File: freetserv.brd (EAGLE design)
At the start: 91.4 x 82.5 mm, 70 parts, among them IC2 SN75240PW, Q1 12MHz, Q2 6MHz, U1 MCP16311-E/MS

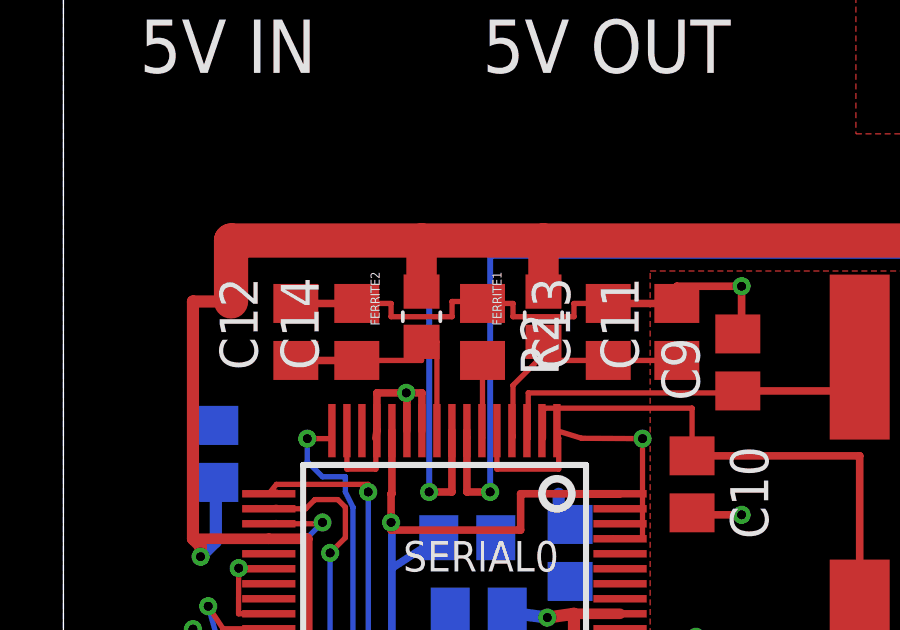
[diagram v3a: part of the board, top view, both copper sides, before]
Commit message: move 100nF capacitors closer to VPHY/VPLL
fixes #11
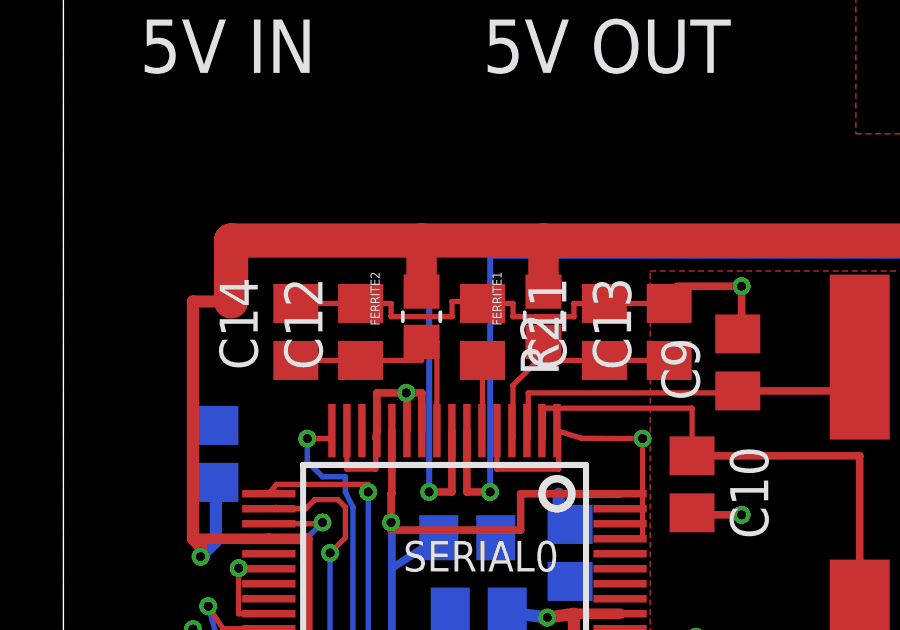
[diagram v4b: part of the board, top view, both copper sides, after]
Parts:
- moved C11 2.41 mm to (18.0, 63.8)
- moved C12 2.16 mm to (9.91, 63.8)
- moved C13 2.03 mm to (20.2, 63.8)
- moved C14 2.03 mm to (7.75, 63.8)
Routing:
- net GND: track 140.1 -> 139.2 mm
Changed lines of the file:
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@@
 <attribute name="PARTNO" value="709-1171-1-ND" x="20.955" y="58.674" size="1.778" layer="27" rot="R270" display="off"/>
 </element>
-<element name="C11" library="resistor" package="C0805" value="0.1uF" x="20.447" y="63.754" rot="R90">
-<attribute name="PARTNO" value="1276-1003-1-ND" x="20.447" y="63.754" size="1.778" layer="27" rot="R90" display="off"/>
-</element>
-<element name="C12" library="resistor" package="C0805" value="0.1uF" x="7.747" y="63.754" rot="R90">
-<attribute name="PARTNO" value="1276-1003-1-ND" x="7.747" y="63.754" size="1.778" layer="27" rot="R90" display="off"/>
-</element>
-<element name="C13" library="resistor" package="C0805" value="4.7uF" x="18.161" y="63.754" rot="R90">
-<attribute name="PARTNO" value="587-1302-1-ND" x="18.161" y="63.754" size="1.778" layer="27" rot="R90" display="off"/>
-</element>
-<element name="C14" library="resistor" package="C0805" value="4.7uF" x="9.779" y="63.754" rot="R90">
-<attribute name="PARTNO" value="587-1302-1-ND" x="9.779" y="63.754" size="1.778" layer="27" rot="R90" display="off"/>
+<element name="C11" library="resistor" package="C0805" value="0.1uF" x="18.034" y="63.754" rot="R90">
+<attribute name="PARTNO" value="1276-1003-1-ND" x="18.034" y="63.754" size="1.778" layer="27" rot="R90" display="off"/>
+</element>
+<element name="C12" library="resistor" package="C0805" value="0.1uF" x="9.906" y="63.754" rot="R90">
+<attribute name="PARTNO" value="1276-1003-1-ND" x="9.906" y="63.754" size="1.778" layer="27" rot="R90" display="off"/>
+</element>
+<element name="C13" library="resistor" package="C0805" value="4.7uF" x="20.193" y="63.754" rot="R90">
+<attribute name="PARTNO" value="587-1302-1-ND" x="20.193" y="63.754" size="1.778" layer="27" rot="R90" display="off"/>
+</element>
+<element name="C14" library="resistor" package="C0805" value="4.7uF" x="7.747" y="63.754" rot="R90">
+<attribute name="PARTNO" value="587-1302-1-ND" x="7.747" y="63.754" size="1.778" layer="27" rot="R90" display="off"/>
 </element>
 <element name="C2" library="resistor" package="C0805" value="10uF" x="30.48" y="74.295">
@@
 <contactref element="C20" pad="1"/>
 <contactref element="C21" pad="1"/>
-<wire x1="7.747" y1="64.704" x2="9.779" y2="64.704" width="0.254" layer="1"/>
 <contactref element="USB_RASPI_PWR" pad="GND"/>
 <contactref element="USB_RASPI_DATA2" pad="GND"/>
@@
 <wire x1="22.606" y1="63.688" x2="22.479" y2="63.688" width="0.254" layer="1"/>
 <wire x1="22.606" y1="65.278" x2="20.447" y2="65.278" width="0.254" layer="1"/>
-<wire x1="20.447" y1="65.278" x2="20.447" y2="64.704" width="0.254" layer="1"/>
-<wire x1="20.447" y1="64.704" x2="18.161" y2="64.704" width="0.254" layer="1"/>
-<wire x1="18.161" y1="64.704" x2="17.018" y2="64.704" width="0.1778" layer="1"/>
 <wire x1="17.018" y1="64.704" x2="17.018" y2="64.262" width="0.1778" layer="1"/>
 <wire x1="17.018" y1="64.262" x2="14.986" y2="64.262" width="0.1778" layer="1"/>
@@
 <wire x1="12.954" y1="64.262" x2="10.922" y2="64.262" width="0.1778" layer="1"/>
 <wire x1="10.922" y1="64.262" x2="10.922" y2="64.704" width="0.1778" layer="1"/>
-<wire x1="10.922" y1="64.704" x2="9.779" y2="64.704" width="0.1778" layer="1"/>
 <wire x1="14.45" y1="60.464" x2="14.45" y2="59.182" width="0.1778" layer="1"/>
 <wire x1="14.45" y1="59.182" x2="16.51" y2="59.182" width="0.1778" layer="1"/>
@@
 <wire x1="16.002" y1="50.292" x2="14.224" y2="50.292" width="0.254" layer="1"/>
 <contactref element="C45" pad="2"/>
+<wire x1="10.922" y1="64.704" x2="9.906" y2="64.704" width="0.1778" layer="1"/>
+<wire x1="9.906" y1="64.704" x2="7.747" y2="64.704" width="0.1778" layer="1"/>
+<wire x1="17.018" y1="64.704" x2="18.034" y2="64.704" width="0.1778" layer="1"/>
+<wire x1="18.034" y1="64.704" x2="20.193" y2="64.704" width="0.1778" layer="1"/>
 </signal>
 <signal name="USB0_DM_P">
@@
 <contactref element="C13" pad="1"/>
 <wire x1="16.002" y1="63.4245" x2="16.002" y2="62.804" width="0.1778" layer="1"/>
-<wire x1="16.002" y1="62.804" x2="18.161" y2="62.804" width="0.1778" layer="1"/>
 <wire x1="16.002" y1="62.804" x2="15.814" y2="62.804" width="0.1778" layer="1"/>
 <wire x1="15.814" y1="62.804" x2="14.986" y2="61.976" width="0.1778" layer="1"/>
 <wire x1="14.986" y1="61.976" x2="14.986" y2="60.246" width="0.1778" layer="1"/>
 <wire x1="14.986" y1="60.246" x2="14.95" y2="60.464" width="0.1778" layer="1"/>
-<wire x1="18.161" y1="62.804" x2="20.447" y2="62.804" width="0.1778" layer="1"/>
+<wire x1="20.193" y1="62.804" x2="18.034" y2="62.804" width="0.1778" layer="1"/>
+<wire x1="18.034" y1="62.804" x2="16.002" y2="62.804" width="0.1778" layer="1"/>
 </signal>
 <signal name="N$18">
@@
 <contactref element="C12" pad="1"/>
 <contactref element="C14" pad="1"/>
-<wire x1="9.779" y1="62.804" x2="7.747" y2="62.804" width="0.254" layer="1"/>
 <wire x1="11.938" y1="63.4245" x2="12.45" y2="63.4245" width="0.1778" layer="1"/>
 <wire x1="12.45" y1="63.4245" x2="12.45" y2="60.464" width="0.1778" layer="1"/>
 <wire x1="11.938" y1="63.4245" x2="11.938" y2="62.804" width="0.1778" layer="1"/>
-<wire x1="11.938" y1="62.804" x2="9.779" y2="62.804" width="0.1778" layer="1"/>
+<wire x1="7.747" y1="62.804" x2="9.906" y2="62.804" width="0.1778" layer="1"/>
+<wire x1="9.906" y1="62.804" x2="11.938" y2="62.804" width="0.1778" layer="1"/>
 </signal>
 <signal name="N$27">

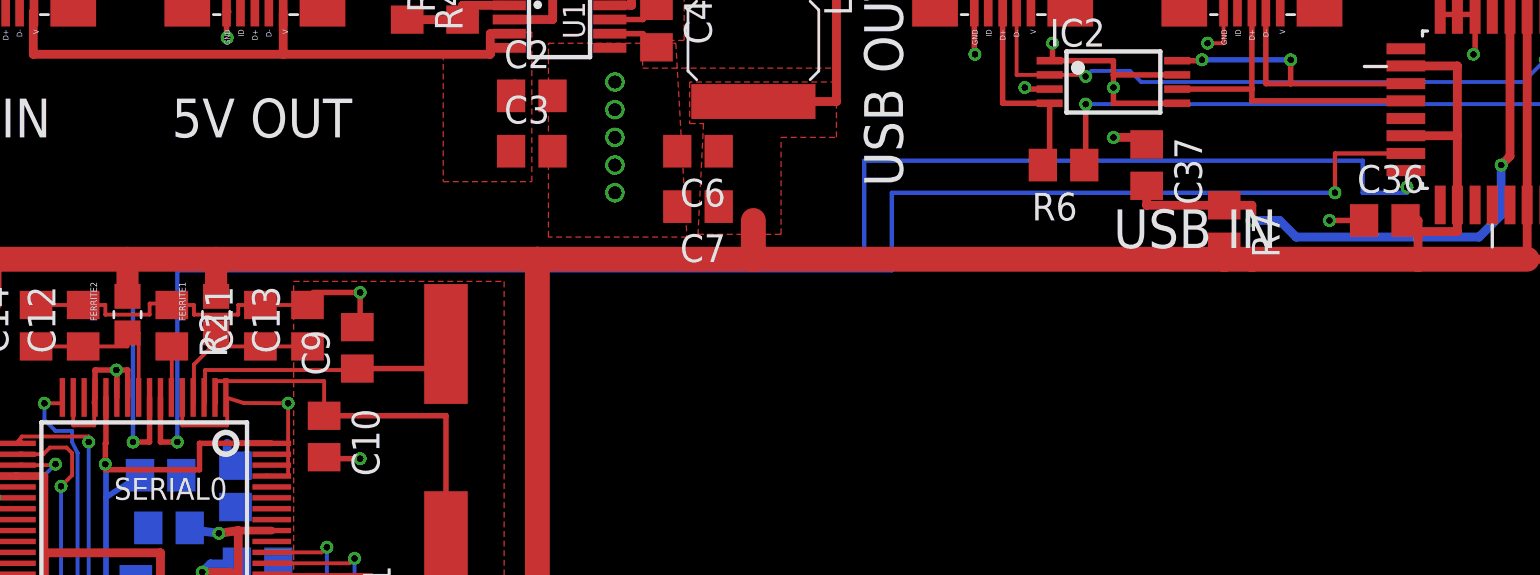
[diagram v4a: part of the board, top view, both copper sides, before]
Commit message: re-route USB as differential pairs with 45° traces
fixes #1
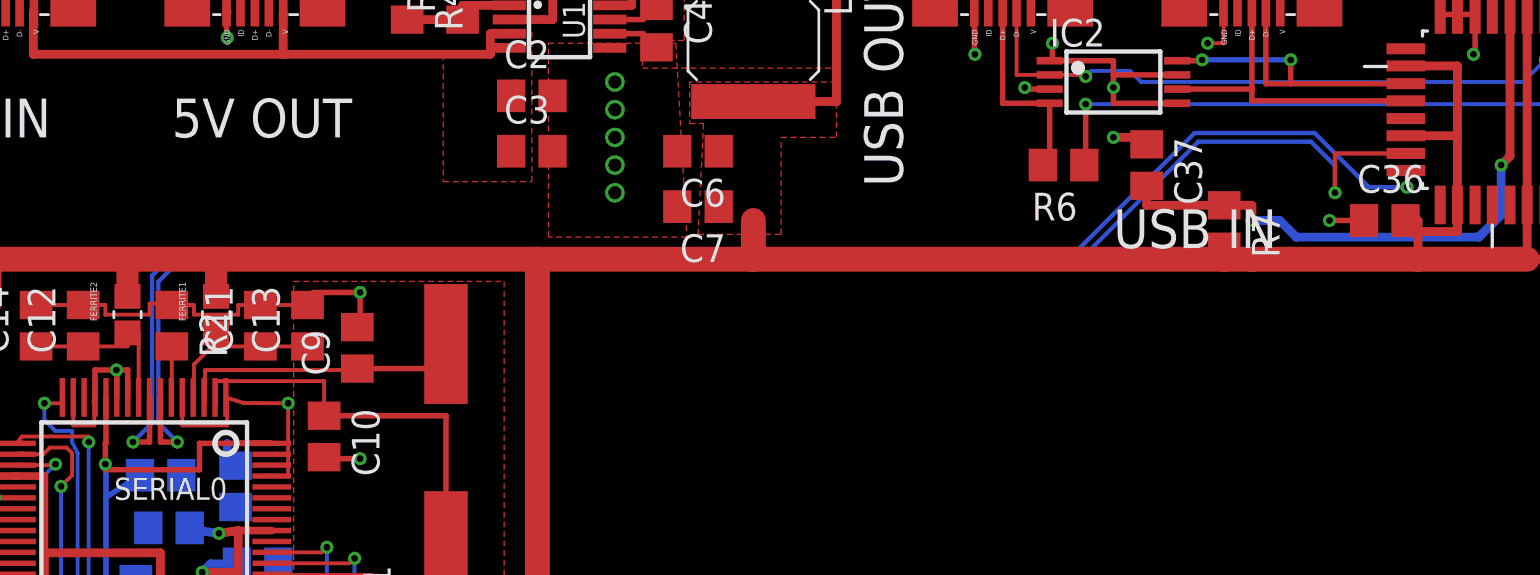
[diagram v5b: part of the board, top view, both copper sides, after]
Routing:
- net USB0_D2_P: track 76.7 -> 72.9 mm
- net USB0_D2_N: track 72.6 -> 74.2 mm
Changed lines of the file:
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@@
 <contactref element="HUB0" pad="15"/>
 <contactref element="SERIAL0" pad="7"/>
-<wire x1="46.99" y1="66.294" x2="14.224" y2="66.294" width="0.2" layer="16"/>
-<wire x1="14.224" y1="66.294" x2="14.224" y2="58.42" width="0.2" layer="16"/>
 <via x="14.224" y="58.42" extent="1-16" drill="0.3048"/>
 <wire x1="13.462" y1="60.21" x2="13.45" y2="60.464" width="0.2" layer="1"/>
 <wire x1="14.224" y1="58.42" x2="13.45" y2="58.42" width="0.254" layer="1"/>
 <wire x1="13.45" y1="58.42" x2="13.45" y2="60.464" width="0.254" layer="1"/>
-<wire x1="46.99" y1="66.294" x2="46.99" y2="69.85" width="0.2" layer="16"/>
-<wire x1="46.99" y1="69.85" x2="67.31" y2="69.85" width="0.2" layer="16"/>
 <via x="67.31" y="69.85" extent="1-16" drill="0.3048"/>
 <wire x1="67.31" y1="69.85" x2="67.31" y2="71.6534" width="0.2" layer="1"/>
 <wire x1="67.31" y1="71.6534" x2="70.5612" y2="71.6534" width="0.2" layer="1"/>
+<wire x1="67.31" y1="69.85" x2="67.31" y2="71.09115625" width="0.2" layer="16"/>
+<wire x1="67.31" y1="71.09115625" x2="66.21115625" y2="72.19" width="0.2" layer="16"/>
+<wire x1="66.21115625" y1="72.19" x2="61.04284375" y2="72.19" width="0.2" layer="16"/>
+<wire x1="61.04284375" y1="72.19" x2="55.45484375" y2="66.602" width="0.2" layer="16"/>
+<wire x1="55.45484375" y1="66.602" x2="14.17984375" y2="66.602" width="0.2" layer="16"/>
+<wire x1="14.17984375" y1="66.602" x2="13.349421875" y2="65.771578125" width="0.2" layer="16"/>
+<wire x1="13.349421875" y1="65.771578125" x2="13.349421875" y2="59.294578125" width="0.2" layer="16"/>
+<wire x1="13.349421875" y1="59.294578125" x2="14.224" y2="58.42" width="0.2" layer="16"/>
 </signal>
 <signal name="USB0_D2_P" class="1">
 <contactref element="HUB0" pad="16"/>
 <contactref element="SERIAL0" pad="8"/>
-<wire x1="45.72" y1="67.056" x2="12.192" y2="67.056" width="0.2" layer="16"/>
-<wire x1="12.192" y1="67.056" x2="12.192" y2="58.42" width="0.2" layer="16"/>
 <via x="12.192" y="58.42" extent="1-16" drill="0.3048"/>
 <wire x1="12.192" y1="58.42" x2="12.95" y2="58.42" width="0.254" layer="1"/>
 <wire x1="12.95" y1="58.42" x2="12.95" y2="60.464" width="0.254" layer="1"/>
-<wire x1="45.72" y1="67.056" x2="45.72" y2="71.32" width="0.2" layer="16"/>
-<wire x1="45.72" y1="71.32" x2="68.58" y2="71.32" width="0.2" layer="16"/>
 <via x="70.612" y="70.104" extent="1-16" drill="0.3048"/>
 <wire x1="70.612" y1="70.104" x2="70.612" y2="70.866" width="0.2" layer="1"/>
 <wire x1="70.612" y1="70.866" x2="70.5612" y2="70.866" width="0.2" layer="1"/>
-<wire x1="68.58" y1="71.32" x2="68.58" y2="69.85" width="0.2" layer="16"/>
-<wire x1="68.58" y1="69.85" x2="70.612" y2="69.85" width="0.2" layer="16"/>
-<wire x1="70.612" y1="69.85" x2="70.612" y2="70.104" width="0.2" layer="16"/>
+<wire x1="70.612" y1="70.104" x2="68.86284375" y2="70.104" width="0.2" layer="16"/>
+<wire x1="68.86284375" y1="70.104" x2="66.37684375" y2="72.59" width="0.2" layer="16"/>
+<wire x1="66.37684375" y1="72.59" x2="60.87715625" y2="72.59" width="0.2" layer="16"/>
+<wire x1="60.87715625" y1="72.59" x2="55.28915625" y2="67.002" width="0.2" layer="16"/>
+<wire x1="55.28915625" y1="67.002" x2="14.01415625" y2="67.002" width="0.2" layer="16"/>
+<wire x1="14.01415625" y1="67.002" x2="13.066578125" y2="66.054421875" width="0.2" layer="16"/>
+<wire x1="13.066578125" y1="66.054421875" x2="13.066578125" y2="59.294578125" width="0.2" layer="16"/>
+<wire x1="13.066578125" y1="59.294578125" x2="12.192" y2="58.42" width="0.2" layer="16"/>
 </signal>
 <signal name="+1V8">

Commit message: add 27Ω resistors to host D+/D- port for impedance matching
fixes #6
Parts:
- added R1, R8: 27, resistor:R0805
- moved R6 20.3 mm to (75.1, 73.5), flipped to the bottom, turned to 0 degrees
- moved IC2 5.11 mm to (62.2, 74.4)
- moved C37 3.61 mm to (55.9, 68.8), turned to 0 degrees
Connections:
- new net N$12: R1.1, USB_RASPI_DATA.D-
- new net N$13: R8.1, USB_RASPI_DATA.D+
- net N$41: now also R8.2; no longer USB_RASPI_DATA.D+
- net USB0_DM_N: now also R1.2; no longer USB_RASPI_DATA.D-
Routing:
- net USB0_DM_P: track 28.9 -> 5.99 mm, vias 2 -> 1
- net N$41: track 9.50 -> 18.4 mm, vias 0 -> 1
- net N$2: track 16.1 -> 9.15 mm, vias 2 -> 0
- net N$13: track 0.00 -> 6.55 mm
- net USB0_DM_N: track 30.0 -> 24.0 mm
- net N$12: track 0.00 -> 4.00 mm
- net N$1: track 14.6 -> 10.9 mm
- net GND: track 139.2 -> 140.5 mm, vias 36 -> 37
- net N$43: track 27.9 -> 29.1 mm

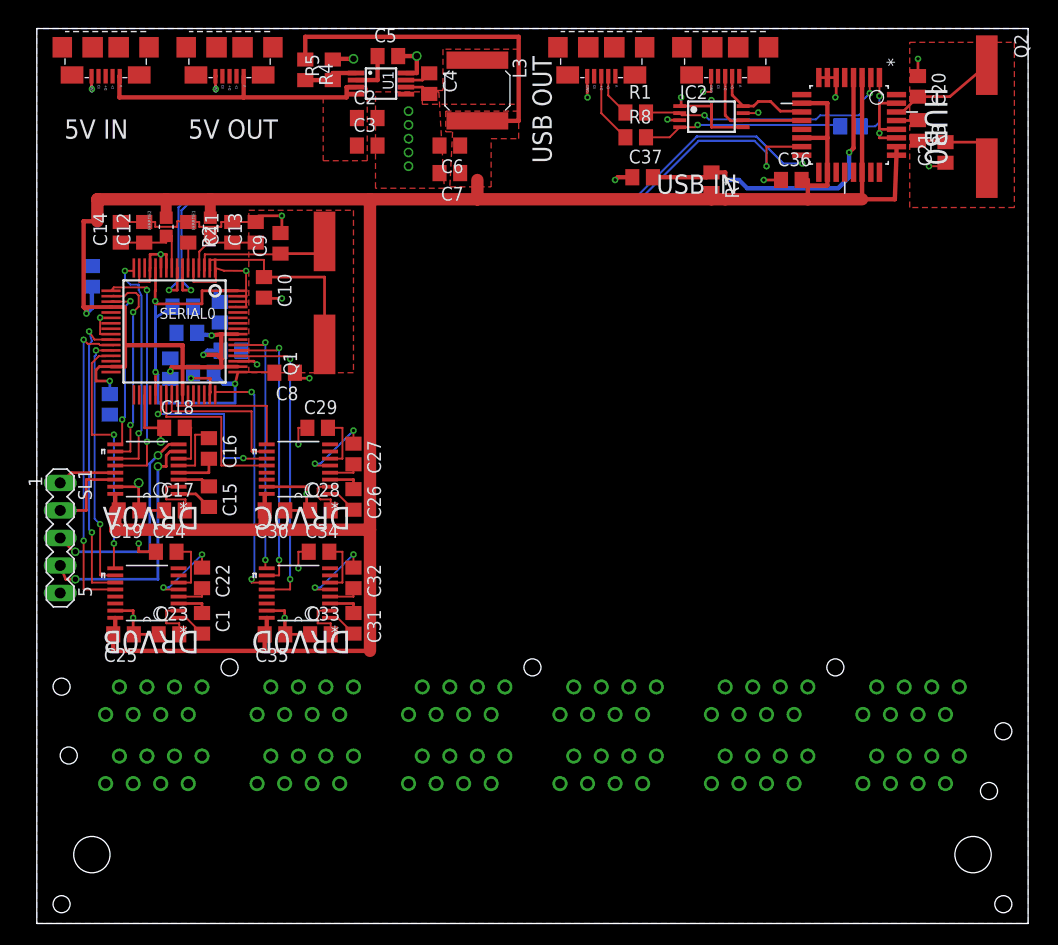
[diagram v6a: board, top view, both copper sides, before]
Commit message: fix remaining DRC errors
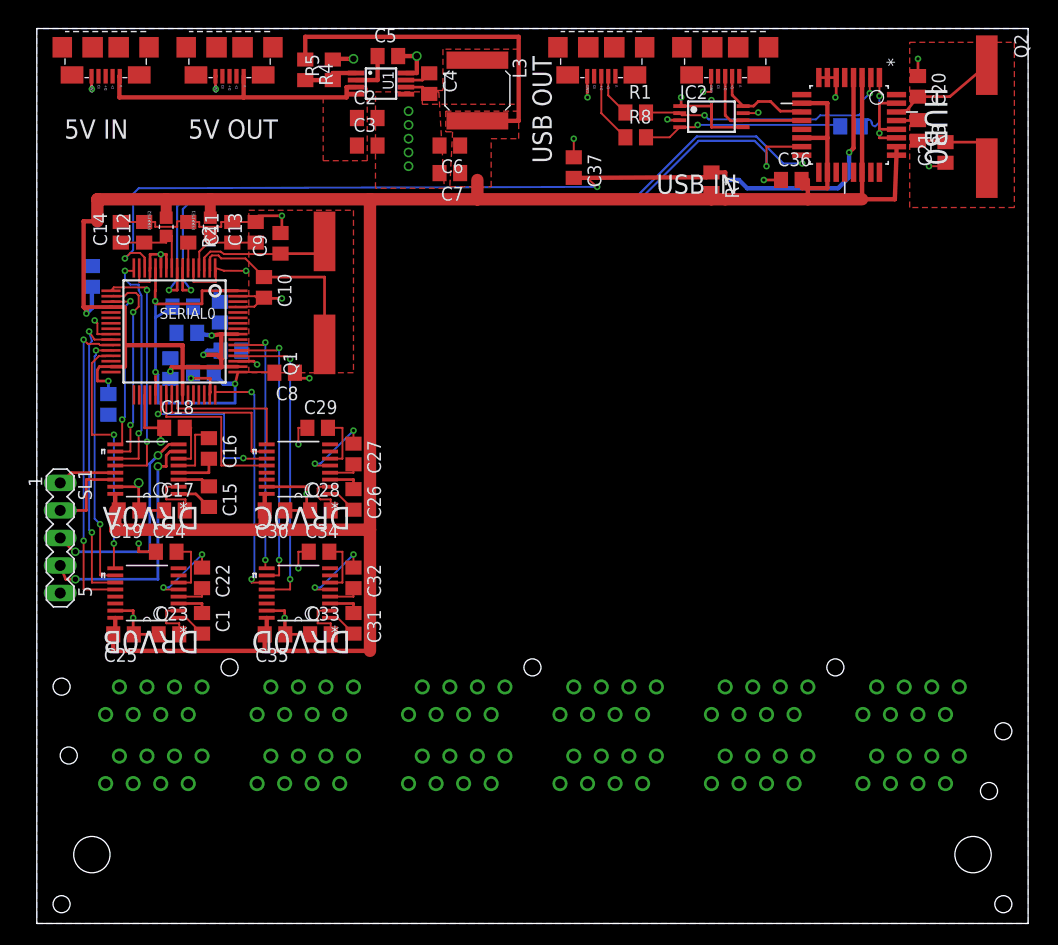
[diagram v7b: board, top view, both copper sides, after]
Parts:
- moved C37 6.41 mm to (49.5, 69.7), turned to 270 degrees
- moved C42 0.13 mm to (6.60, 47.9)
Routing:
- net N$43: track 29.1 -> 91.3 mm, vias 2 -> 4
- net USB0_DM_P: track 5.99 -> 6.51 mm
- net N$48: track 22.8 -> 23.3 mm
